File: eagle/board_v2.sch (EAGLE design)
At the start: 36 parts, among them J1 RJ11-4X, J2 RJ11-4X, Q1 BD140, Q10 BD140, Q11 BD140, Q12 BD140, Q13 BD140, Q14 BD140, Q15 BD140, Q2 BD140, Q3 BD140, Q4 BD140, Q5 BD140, Q6 BD140, Q7 BD140, Q8 BD140, Q9 BD140, X10 22-23-2041, X6 22-23-2041, X7 22-23-2041, X8 22-23-2041, X9 22-23-2041

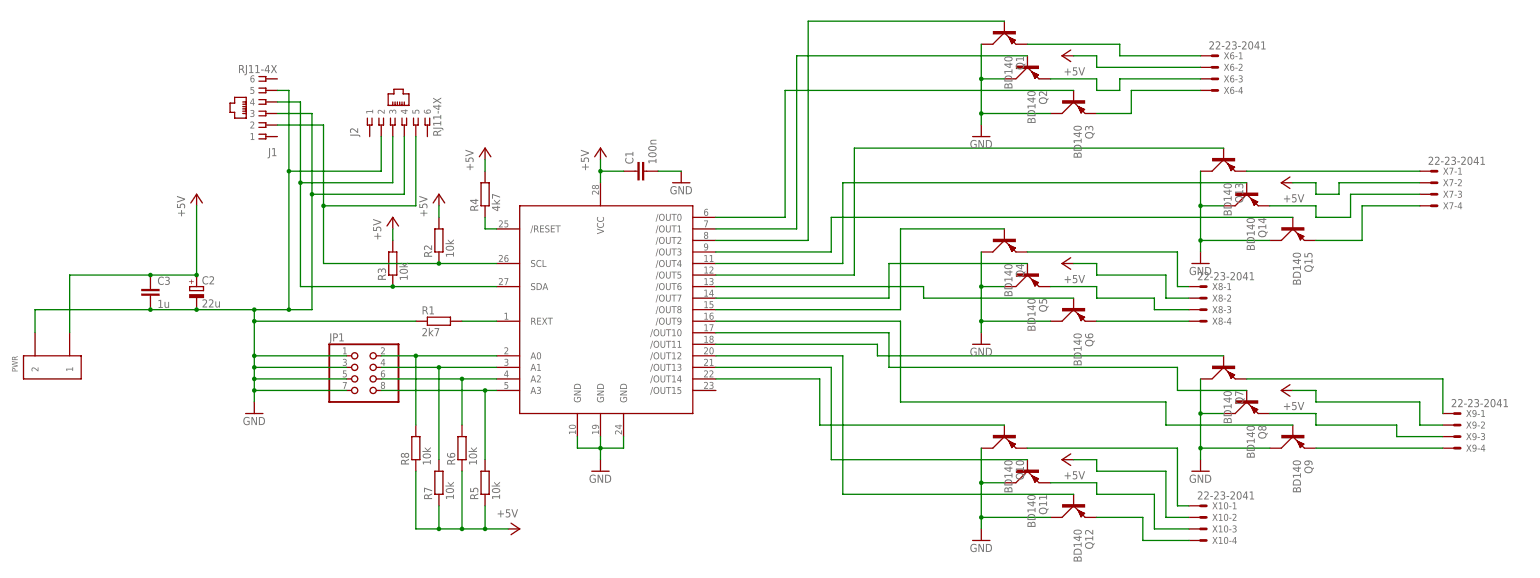
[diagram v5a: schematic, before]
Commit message: board v2.2 - silkscreen cleanup
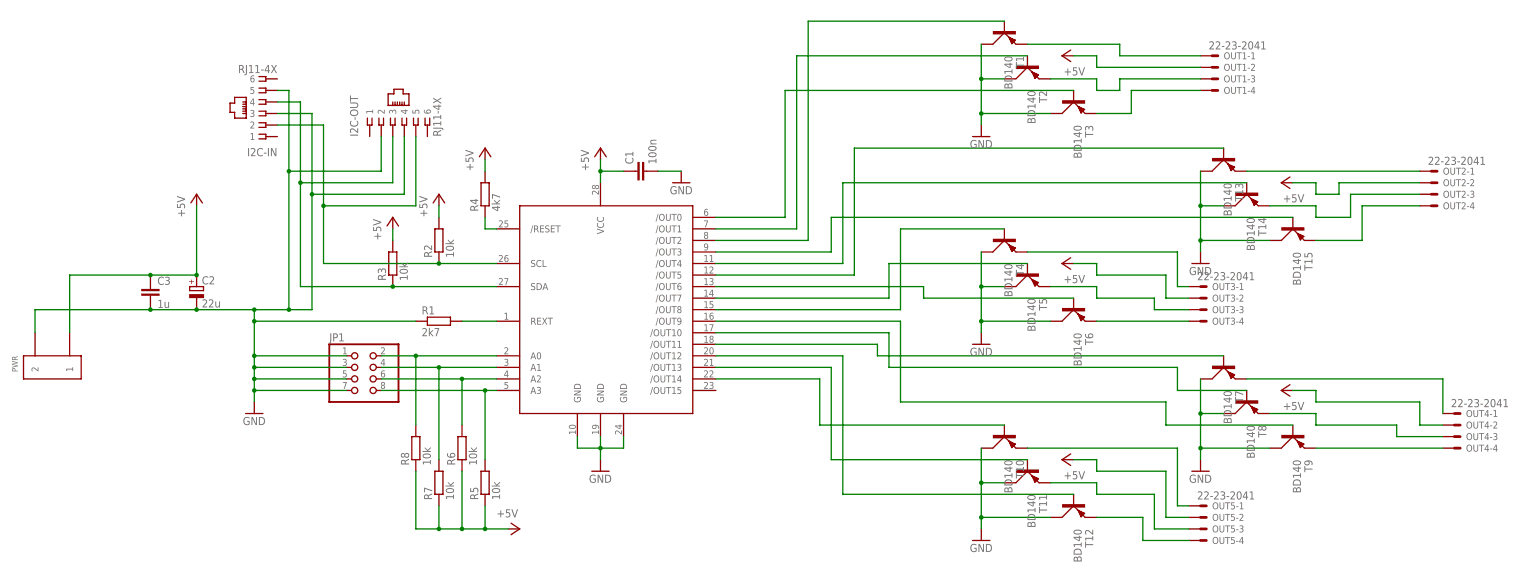
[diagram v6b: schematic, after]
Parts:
- renumbered J1 to I2C-IN, J2 to I2C-OUT, Q1 to T1, Q10 to T10, Q11 to T11, Q12 to T12, Q13 to T13, Q14 to T14, Q15 to T15, Q2 to T2, Q3 to T3, Q4 to T4, Q5 to T5, Q6 to T6, Q7 to T7, Q8 to T8, Q9 to T9, U$1 to IC1, X10 to OUT5, X6 to OUT1, X7 to OUT2, X8 to OUT3, X9 to OUT4

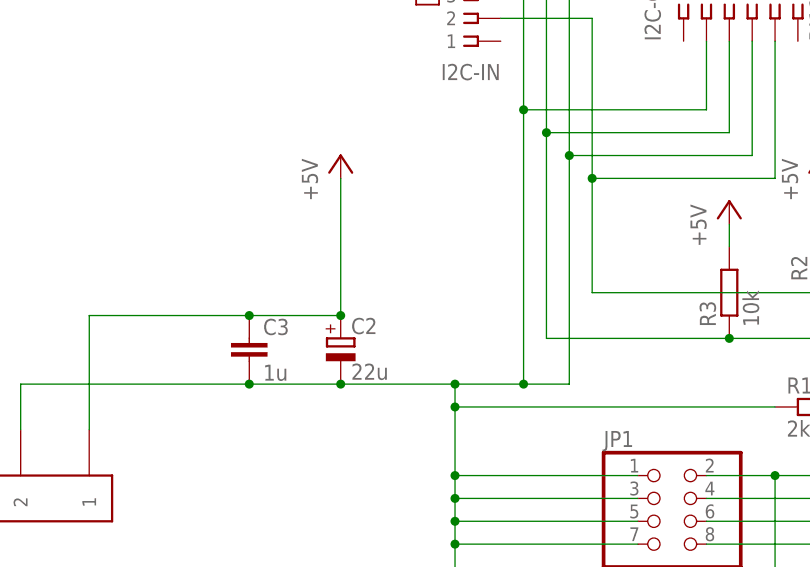
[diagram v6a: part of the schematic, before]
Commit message: Board v2.2 - power-on LED added; minor adjustments to silkscreen (version, brmlab logo)
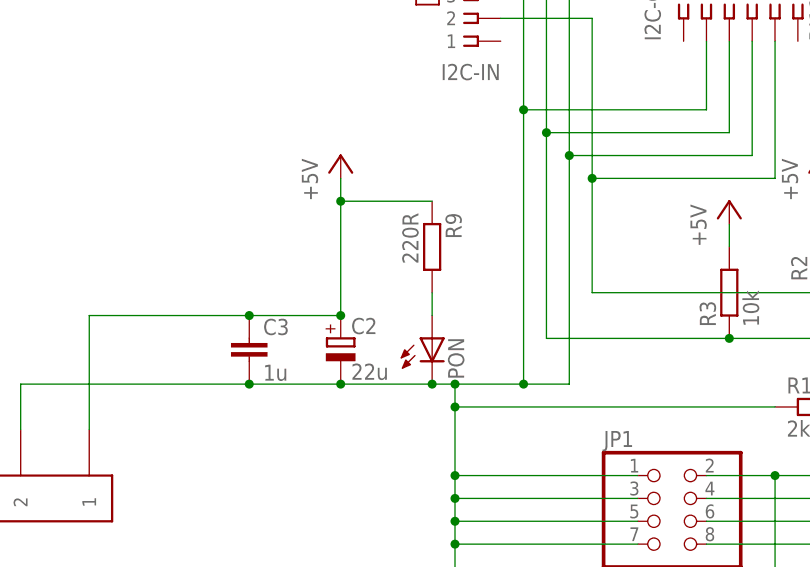
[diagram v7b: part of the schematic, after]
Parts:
- added PON: (no value), led:LEDCHIPLED_1206
- added R9: 220R, resistor:R-EU_R1206
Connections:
- new net N$39: PON.A, R9.2
- net +5V: now also R9.1
- net GND: now also PON.C
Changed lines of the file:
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@@
 <part name="OUT5" library="con-molex" deviceset="22-23-2041" device=""/>
 <part name="C3" library="resistor" deviceset="C-EU" device="C1206" value="1u"/>
+<part name="PON" library="led" deviceset="LED" device="CHIPLED_1206"/>
+<part name="R9" library="resistor" deviceset="R-EU_" device="R1206" value="220R"/>
 </parts>
 <sheets>
@@
 <instance part="OUT5" gate="-4" x="177.8" y="12.7"/>
 <instance part="C3" gate="G$1" x="-53.34" y="68.58"/>
+<instance part="PON" gate="G$1" x="-33.02" y="68.58"/>
+<instance part="R9" gate="G$1" x="-33.02" y="78.74" rot="R270"/>
 </instances>
 <busses>
@@
 <pinref part="P+10" gate="1" pin="+5V"/>
 <pinref part="C2" gate="G$1" pin="+"/>
-<wire x1="-43.18" y1="86.36" x2="-43.18" y2="71.12" width="0.1524" layer="91"/>
+<wire x1="-43.18" y1="86.36" x2="-43.18" y2="83.82" width="0.1524" layer="91"/>
 <junction x="-43.18" y="71.12"/>
+<wire x1="-43.18" y1="83.82" x2="-43.18" y2="71.12" width="0.1524" layer="91"/>
 <wire x1="-43.18" y1="71.12" x2="-53.34" y2="71.12" width="0.1524" layer="91"/>
 <pinref part="C3" gate="G$1" pin="1"/>
@@
 <wire x1="-53.34" y1="71.12" x2="-71.12" y2="71.12" width="0.1524" layer="91"/>
 <wire x1="-71.12" y1="71.12" x2="-71.12" y2="58.42" width="0.1524" layer="91"/>
+<pinref part="R9" gate="G$1" pin="1"/>
+<wire x1="-33.02" y1="83.82" x2="-43.18" y2="83.82" width="0.1524" layer="91"/>
+<junction x="-43.18" y="83.82"/>
 </segment>
 <segment>
@@
 <wire x1="-78.74" y1="63.5" x2="-53.34" y2="63.5" width="0.1524" layer="91"/>
 <wire x1="-53.34" y1="63.5" x2="-43.18" y2="63.5" width="0.1524" layer="91"/>
-<wire x1="-43.18" y1="63.5" x2="-30.48" y2="63.5" width="0.1524" layer="91"/>
+<wire x1="-43.18" y1="63.5" x2="-33.02" y2="63.5" width="0.1524" layer="91"/>
+<wire x1="-33.02" y1="63.5" x2="-30.48" y2="63.5" width="0.1524" layer="91"/>
 <wire x1="-30.48" y1="63.5" x2="-22.86" y2="63.5" width="0.1524" layer="91"/>
 <wire x1="-22.86" y1="63.5" x2="-17.78" y2="63.5" width="0.1524" layer="91"/>
@@
 <pinref part="PWR" gate="G$1" pin="2"/>
 <wire x1="-78.74" y1="63.5" x2="-78.74" y2="58.42" width="0.1524" layer="91"/>
+<pinref part="PON" gate="G$1" pin="C"/>
+<junction x="-33.02" y="63.5"/>
 </segment>
 <segment>
@@
 </segment>
 </net>
+<net name="N$39" class="0">
+<segment>
+<pinref part="PON" gate="G$1" pin="A"/>
+<pinref part="R9" gate="G$1" pin="2"/>
+<wire x1="-33.02" y1="73.66" x2="-33.02" y2="71.12" width="0.1524" layer="91"/>
+</segment>
+</net>
